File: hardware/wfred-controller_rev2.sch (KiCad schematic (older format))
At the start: 12 parts, among them IC201 ATMEGA328P-A, P201 ISP, X201 14.7456MHz

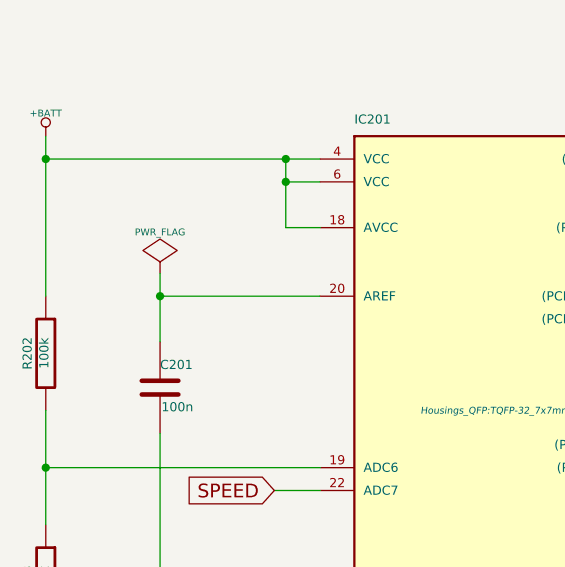
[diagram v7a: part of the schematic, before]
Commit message: Fixed ERC errors
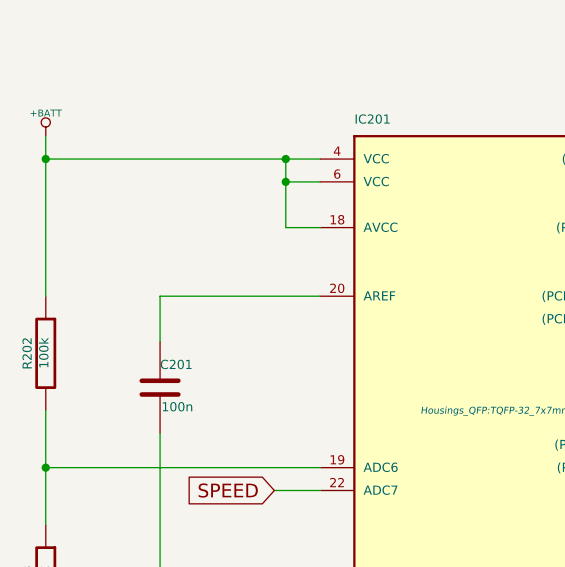
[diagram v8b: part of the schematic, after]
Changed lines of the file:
@@
 MOSI
 $Comp
-L PWR_FLAG #FLG013
-U 1 1 59214642
-P 3300 3700
-F 0 "#FLG013" H 3300 3795 30  0001 C CNN
-F 1 "PWR_FLAG" H 3300 3880 30  0000 C CNN
-F 2 "" H 3300 3700 60  0001 C CNN
-F 3 "" H 3300 3700 60  0001 C CNN
-	1    3300 3700
-	1    0    0    -1
-$EndComp
-$Comp
-L GND-RESCUE-wfred_rev2 #PWR014
+L GND-RESCUE-wfred_rev2 #PWR012
 U 1 1 5920D54C
 P 10600 4100
-F 0 "#PWR014" H 10600 4100 30  0001 C CNN
+F 0 "#PWR012" H 10600 4100 30  0001 C CNN
 F 1 "GND" H 10600 4030 30  0001 C CNN
 F 2 "" H 10600 4100 60  0001 C CNN
@@
 $EndComp
 $Comp
-L GND-RESCUE-wfred_rev2 #PWR015
+L GND-RESCUE-wfred_rev2 #PWR013
 U 1 1 5920D60E
 P 5300 2600
-F 0 "#PWR015" H 5300 2600 30  0001 C CNN
+F 0 "#PWR013" H 5300 2600 30  0001 C CNN
 F 1 "GND" H 5300 2530 30  0001 C CNN
 F 2 "" H 5300 2600 60  0001 C CNN
@@
 LED_FORWARD
 $Comp
-L GND-RESCUE-wfred_rev2 #PWR016
+L GND-RESCUE-wfred_rev2 #PWR014
 U 1 1 592F4690
 P 3300 5700
-F 0 "#PWR016" H 3300 5700 30  0001 C CNN
+F 0 "#PWR014" H 3300 5700 30  0001 C CNN
 F 1 "GND" H 3300 5630 30  0001 C CNN
 F 2 "" H 3300 5700 60  0001 C CNN
@@
 $EndComp
 $Comp
-L GND-RESCUE-wfred_rev2 #PWR017
+L GND-RESCUE-wfred_rev2 #PWR015
 U 1 1 5A171EC6
 P 9500 4100
-F 0 "#PWR017" H 9500 4100 30  0001 C CNN
+F 0 "#PWR015" H 9500 4100 30  0001 C CNN
 F 1 "GND" H 9500 4030 30  0001 C CNN
 F 2 "" H 9500 4100 60  0001 C CNN
@@
 $EndComp
 $Comp
-L GND-RESCUE-wfred_rev2 #PWR018
+L GND-RESCUE-wfred_rev2 #PWR016
 U 1 1 5A171EEF
 P 9300 3300
-F 0 "#PWR018" H 9300 3300 30  0001 C CNN
+F 0 "#PWR016" H 9300 3300 30  0001 C CNN
 F 1 "GND" H 9300 3230 30  0001 C CNN
 F 2 "" H 9300 3300 60  0001 C CNN
@@
 $EndComp
 $Comp
-L +BATT #PWR019
+L +BATT #PWR017
 U 1 1 5BE0B208
 P 2800 3100
-F 0 "#PWR019" H 2800 3050 20  0001 C CNN
+F 0 "#PWR017" H 2800 3050 20  0001 C CNN
 F 1 "+BATT" H 2800 3200 30  0000 C CNN
 F 2 "" H 2800 3100 60  0001 C CNN
@@
 Connection ~ 10600 3900
 Wire Wire Line
-	3300 3700 3300 4000
-Wire Wire Line
 	3300 4400 3300 5700
 Wire Wire Line
@@
 Wire Wire Line
 	4900 2100 4800 2100
-Connection ~ 3300 3800
 Connection ~ 5400 1600
 Wire Wire Line
@@
 Connection ~ 3850 3300
 $Comp
-L GND-RESCUE-wfred_rev2 #PWR020
+L GND-RESCUE-wfred_rev2 #PWR018
 U 1 1 5BE232F3
 P 2800 5700
-F 0 "#PWR020" H 2800 5700 30  0001 C CNN
+F 0 "#PWR018" H 2800 5700 30  0001 C CNN
 F 1 "GND" H 2800 5630 30  0001 C CNN
 F 2 "" H 2800 5700 60  0001 C CNN
@@
 Connection ~ 2800 4550
 $Comp
-L VCC #PWR021
+L VCC #PWR019
 U 1 1 5BE4849E
 P 5400 1400
-F 0 "#PWR021" H 5400 1500 30  0001 C CNN
+F 0 "#PWR019" H 5400 1500 30  0001 C CNN
 F 1 "VCC" H 5400 1500 30  0000 C CNN
 F 2 "" H 5400 1400 60  0001 C CNN
@@
 	1    0    0    -1
 $EndComp
+Wire Wire Line
+	3300 3800 3300 4000
 $EndSCHEMATC
